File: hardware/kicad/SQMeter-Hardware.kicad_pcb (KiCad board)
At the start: 2 copper layers, 125 x 82 mm, 62 parts, among them J1 12V IN, J10 AUX, J2 USB-C, J3 I2C TSL2591, J4 I2C MLX90614, J5 I2C BME280, J6 I2C SPARE, J7 GPS, J8 RG-15, J9 WIND, Q1 AO3401A, SW1 RESET, SW2 BOOT, U1 AP63203WU, U2 USBLC6-2SC6, U3 ESP32-S3-WROOM-1-N16R8, U4 USBLC6-2SC6, U5 USBLC6-2SC6, U6 USBLC6-2SC6

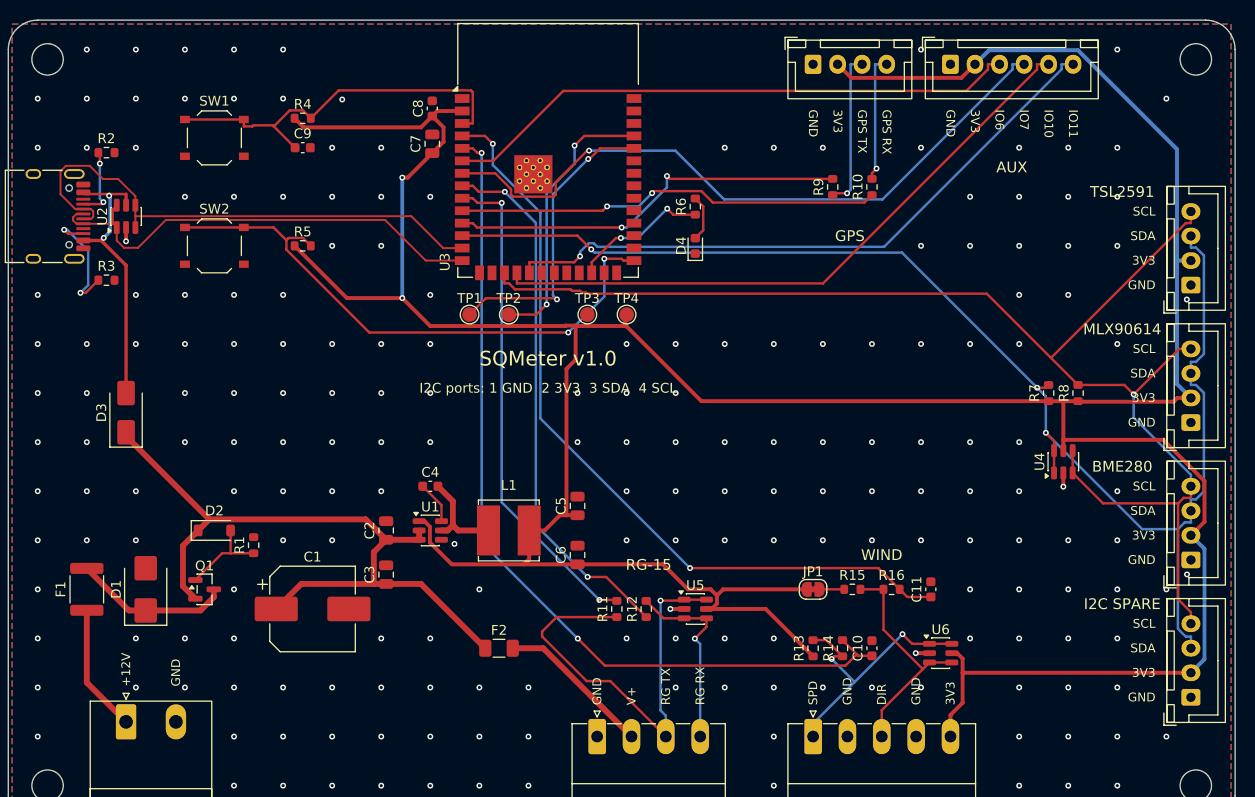
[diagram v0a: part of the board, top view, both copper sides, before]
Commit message: feat: DevKitC-1 socket variant, verified LCSC parts, JLC fab exports
- SQM_VARIANT=devkit swaps the soldered module for ESP32-S3-DevKitC-1 sockets
  (header geometry from Espressif's DXF), 5 V buck feeding the DevKit 5V pin,
  antenna keepout and silkscreen outline
- every part has an in-stock LCSC number; polyfuses moved to 24 V parts
- export_jlc.sh writes gerber zip, BOM and CPL per variant
- build retries routing until DRC has no unconnected or dangling items
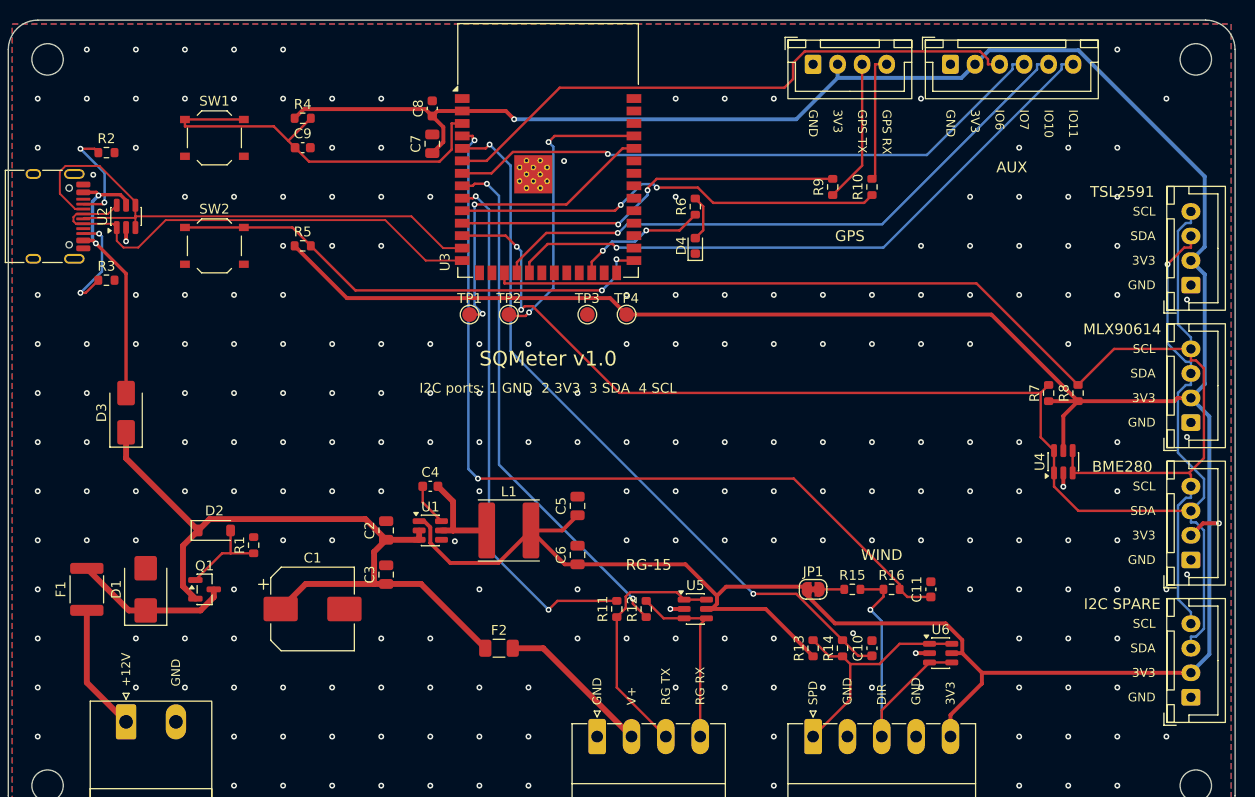
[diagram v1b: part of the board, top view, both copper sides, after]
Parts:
- C1: footprint Capacitor_SMD:CP_Elec_8x10.5 -> Capacitor_SMD:CP_Elec_8x10
- F1: value 1.5A -> 1.5A 24V
- F2: value 0.5A -> 0.5A 24V
- L1: value 4.7u 3A -> 4.7u 3.3A; footprint Inductor_SMD:L_Bourns_SRN6045TA -> Inductor_SMD:L_Sunlord_SWPA6045S
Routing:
- net +3V3: track 369.3 -> 392.7 mm
- net /RG_TXO: track 44.4 -> 25.4 mm, vias 1 -> 0
- net /WIND_SPD: track 89.4 -> 74.6 mm
- net /BOOT: track 59.1 -> 50.8 mm
- net /WIND_DIR: track 80.8 -> 88.2 mm
- net /AUX2: track 69.3 -> 62.4 mm
- net /WDIR_EXT: track 24.0 -> 30.2 mm, vias 0 -> 1
- net /SDA: track 140.4 -> 144.5 mm
- net /RG_RX: track 50.6 -> 54.0 mm
- net /CC1: track 7.40 -> 10.7 mm
- net /EN: track 39.7 -> 42.9 mm
- net /SCL: track 140.4 -> 137.3 mm, vias 1 -> 0
- net /WSPD_EXT: track 27.9 -> 25.0 mm, vias 2 -> 0
- net /USB_DN: track 55.0 -> 57.4 mm
- net /AUX1: track 59.1 -> 61.2 mm
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
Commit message: feat: Waveshare ESP32-S3-Zero socket variant and one GPIO map for all boards
- SQM_VARIANT=zero: ESP32-S3-Zero-M on 2x9 sockets (Waveshare pinout and
  drawing), same 5 V feed scheme as the DevKit variant
- GPIO map unified across module, DevKit and Zero (limited by the Zero's
  GPIO1-13 headers): RG-15 1/2, wind 4/5, I2C 8/9, GPS 12/13, AUX 6/7/10/11
- fab exports for all three
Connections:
- U3 pad 10: /GPS_TX -> (no net)
- U3 pad 11: /GPS_RX -> (no net)
- U3 pad 20: (no net) -> /GPS_TX
- U3 pad 21: (no net) -> /GPS_RX
- U3 pad 38: (no net) -> /RG_RX
- U3 pad 39: (no net) -> /RG_TX
- U3 pad 8: /RG_TX -> (no net)
- U3 pad 9: /RG_RX -> (no net)
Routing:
- net +3V3: track 392.7 -> 334.6 mm, vias 2 -> 4
- net /RG_TX: track 53.5 -> 72.9 mm
- net /RG_RX: track 54.0 -> 71.1 mm, vias 2 -> 4
- net /WIND_SPD: track 74.6 -> 89.0 mm
- net /SCL: track 137.3 -> 149.8 mm
- net /WIND_DIR: track 88.2 -> 77.8 mm
- net /AUX1: track 61.2 -> 68.8 mm, vias 0 -> 2
- net /GPS_RX: track 40.2 -> 33.0 mm
- net /BOOT: track 50.8 -> 57.7 mm
- net /EN: track 42.9 -> 36.2 mm
- net /WDIR_EXT: track 30.2 -> 23.9 mm
- net /U0RXD: track 31.5 -> 25.6 mm
- net /GPS_TX: track 44.0 -> 38.4 mm, vias 2 -> 0
- net /U0TXD: track 29.8 -> 34.9 mm
- net /AUX3: track 63.9 -> 67.9 mm, vias 1 -> 2
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
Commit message: fix: centre boards on the A4 sheet instead of hanging off the page origin
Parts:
- moved C1 107.2 mm to (117.0, 124.0)
- moved C10 107.2 mm to (174.0, 128.0)
- moved C11 107.2 mm to (180.0, 122.0)
- moved C2 107.2 mm to (124.5, 116.0)
- moved C3 107.2 mm to (124.5, 120.5)
- moved C4 107.2 mm to (129.0, 111.5)
- moved C5 107.2 mm to (144.0, 113.5)
- moved C6 107.2 mm to (144.0, 118.5)
- moved C8 107.2 mm to (129.2, 73.0)
- moved C9 107.2 mm to (116.0, 77.0)
- moved D1 107.2 mm to (100.0, 122.0)
- moved D2 107.2 mm to (107.0, 116.0)
- moved D3 107.2 mm to (98.0, 104.0)
- moved D4 107.2 mm to (156.0, 87.0)
- moved F1 107.2 mm to (94.0, 122.0)
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
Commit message: feat: second I2C bus for a second TSL2591 (SQM + SQM-L)
TSL2591 has a fixed address, so the second sensor gets its own bus on
GPIO10/11 (I2C-2 JST-XH port, own pull-ups and ESD). AUX drops to IO6/IO7.
Q1 gate zener replaced by a resistor divider (one fewer extended part).
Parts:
- removed D2: BZT52C10, Diode_SMD:D_SOD-123
- added J13: I2C-2 TSL2591 #2, Connector_JST:JST_XH_B4B-XH-A_1x04_P2.50mm_Vertical, F.Cu at (195.0, 68.5)
- added R19: 10k, Resistor_SMD:R_0603_1608Metric, F.Cu at (107.0, 115.0)
- added R20: 4.7k, Resistor_SMD:R_0603_1608Metric, F.Cu at (185.0, 82.5)
- added R21: 4.7k, Resistor_SMD:R_0603_1608Metric, F.Cu at (188.0, 82.5)
- added U7: USBLC6-2SC6, Package_TO_SOT_SMD:SOT-23-6, F.Cu at (192.0, 85.0)
- J10: footprint Connector_JST:JST_XH_B6B-XH-A_1x06_P2.50mm_Vertical -> Connector_JST:JST_XH_B4B-XH-A_1x04_P2.50mm_Vertical
- J3: value I2C TSL2591 -> I2C TSL2591 #1
- moved H2 7.52 mm to (207.5, 75.5)
- moved J10 0.50 mm to (181.5, 68.5)
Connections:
- U3 pad 18: /AUX3 -> /SDA2
- U3 pad 19: /AUX4 -> /SCL2
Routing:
- net /SDA2: track 0.00 -> 88.8 mm, vias 0 -> 2
- net /SCL2: track 0.00 -> 86.3 mm
- net /AUX3: track 67.9 -> 0.00 mm, vias 2 -> 0
- net /AUX4: track 67.5 -> 0.00 mm, vias 1 -> 0
- net +3V3: track 334.6 -> 353.0 mm, vias 4 -> 6
- net /RG_TX: track 72.9 -> 55.6 mm
- net /WIND_DIR: track 77.8 -> 94.7 mm
- net /RG_RX: track 71.1 -> 55.8 mm, vias 4 -> 2
- net /EN: track 36.2 -> 51.2 mm
- net /SCL: track 149.8 -> 138.8 mm, vias 0 -> 1
- net /AUX1: track 68.8 -> 58.6 mm, vias 2 -> 1
- net /SDA: track 148.3 -> 142.0 mm
- net /WIND_SPD: track 89.0 -> 82.8 mm
- net /U0TXD: track 34.9 -> 30.2 mm
- net /BOOT: track 57.7 -> 53.3 mm
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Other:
- board text added: "I2C-2"
- board text added: "TSL2591 #1"
- board text removed: "IO10"
- board text removed: "IO11"
- board text removed: "TSL2591"

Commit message: feat: brand lockup on silkscreen, hardware Rev A, JLC-ready gerber zips
- SQMeter lockup (brand kit silkscreen mark + Inter SemiBold name) as plain
  silkscreen polygons from brand_silk.json; no font install needed
- HW_REV = A: on the silkscreen, KiCad title blocks, gerber metadata and fab
  file names; versioned separately from firmware
- drop the verbose I2C pinout line; per-pin labels already cover it
- gerber zip holds only fab layers + drill files
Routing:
- net /SCL: track 138.8 -> 155.4 mm, vias 1 -> 0
- net /SCL2: track 86.3 -> 99.0 mm, vias 0 -> 1
- net /WIND_SPD: track 82.8 -> 94.9 mm
- net +3V3: track 353.0 -> 363.1 mm, vias 6 -> 5
- net /GPS_TX: track 39.4 -> 48.1 mm, vias 0 -> 2
- net /WIND_DIR: track 94.7 -> 86.9 mm
- net /RG_RXI: track 23.2 -> 30.7 mm
- net /EN: track 51.2 -> 45.3 mm
- net /RG_TXO: track 28.1 -> 23.7 mm, vias 0 -> 1
- net /AUX1: track 58.6 -> 62.4 mm, vias 1 -> 0
- net /U0TXD: track 30.2 -> 26.7 mm
- net /U0RXD: track 25.5 -> 28.7 mm
- net /BOOT: track 53.3 -> 50.3 mm
- net /RG_RX: track 55.8 -> 53.7 mm
- net /WSPD_EXT: track 28.0 -> 26.1 mm
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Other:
- board text added: "Rev A ESP32-S3 module"
- board text removed: "I2C ports: 1 GND 2 3V3 3 SDA 4 SCL"
- board text removed: "SQMeter v1.0"

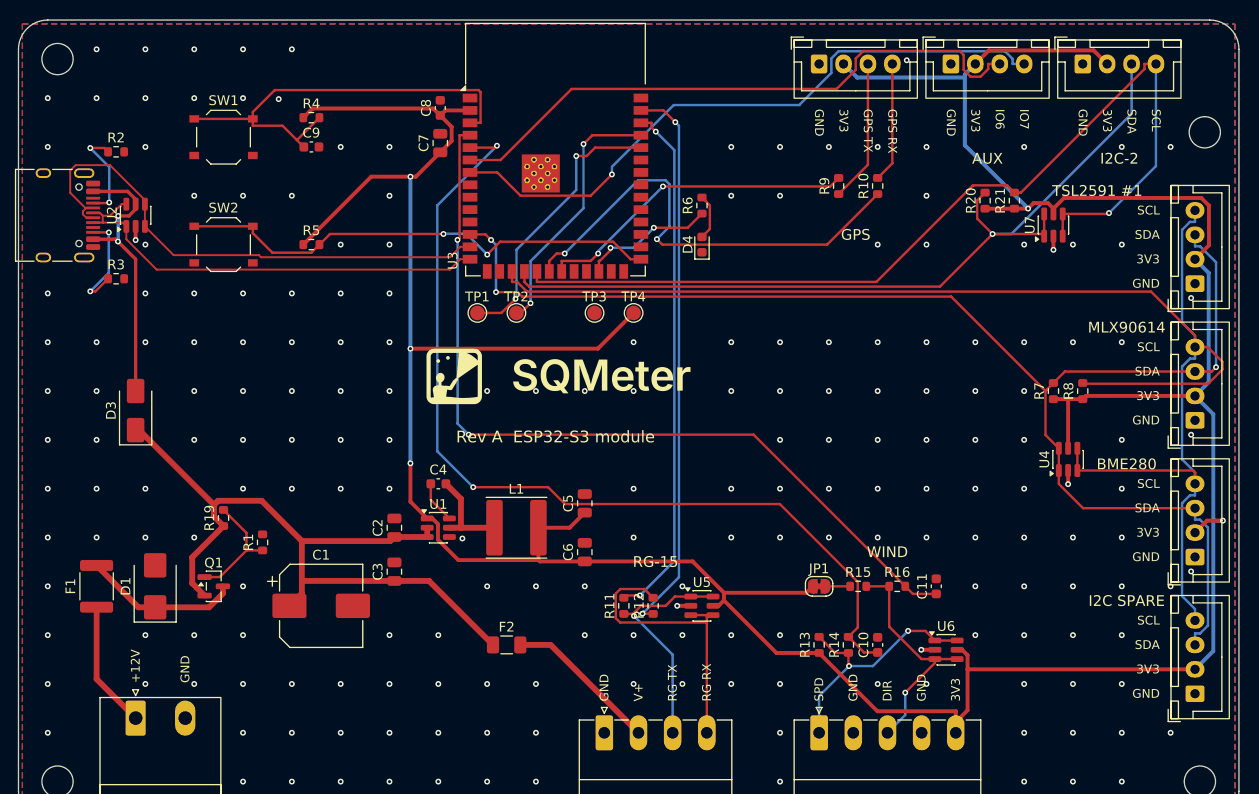
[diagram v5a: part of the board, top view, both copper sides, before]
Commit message: feat: Inter Bold silkscreen (embedded), black mask / white silk stackup
- all silkscreen text and references in Inter Bold, min 1.2 mm; font embedded in
  the board files so they open the same without Inter installed
- stroke widths measured on plotted gerbers (>0.15 mm); KiCad's TrueType
  thickness check ignored as it flags every size of the variable font
- stackup: black solder mask, white silkscreen (3D view; colour is picked at order)
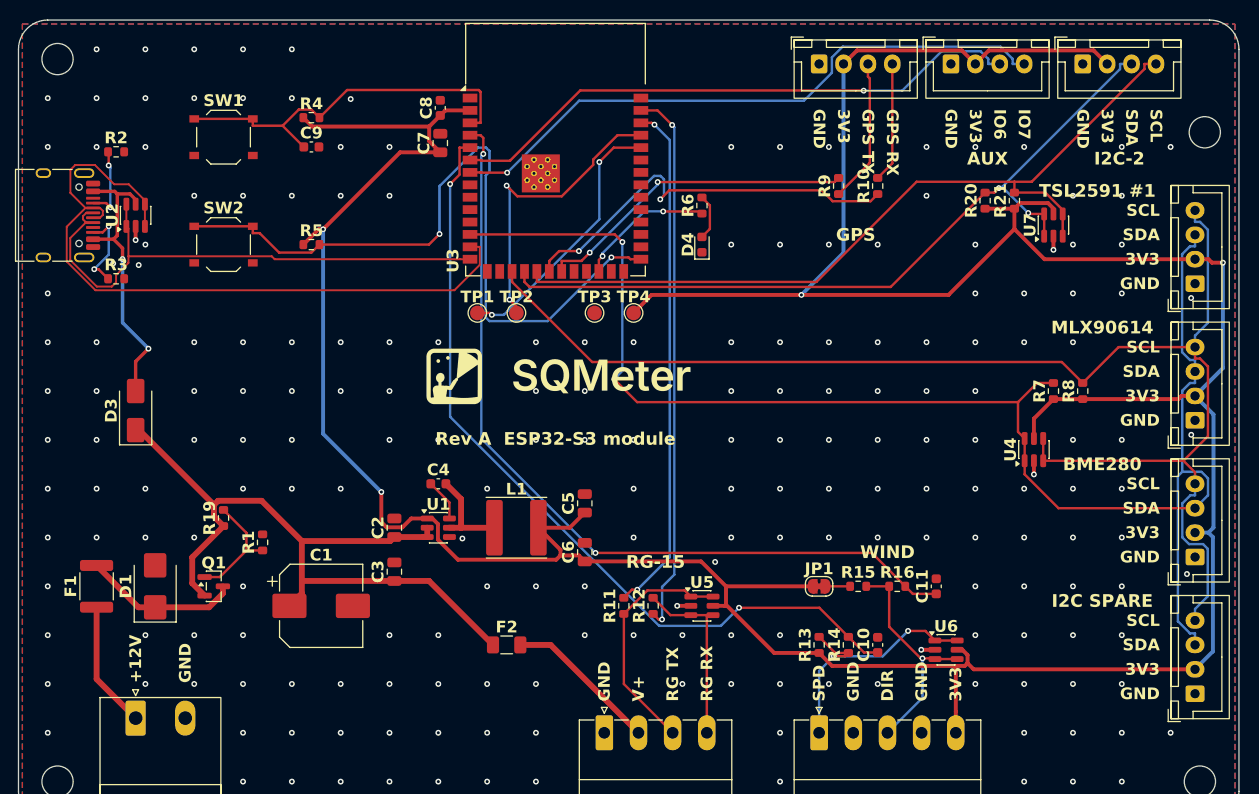
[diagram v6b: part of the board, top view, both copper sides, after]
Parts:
- moved U4 3.64 mm to (190.0, 108.0)
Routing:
- net +3V3: track 363.1 -> 388.9 mm, vias 5 -> 4
- net /BOOT: track 50.3 -> 75.3 mm
- net /USB_DN: track 54.7 -> 73.7 mm
- net /SCL2: track 99.0 -> 83.5 mm, vias 1 -> 0
- net /SDA: track 142.4 -> 155.9 mm, vias 3 -> 2
- net /SCL: track 155.4 -> 142.5 mm
- net /RG_RXI: track 30.7 -> 18.9 mm
- net /WIND_SPD: track 94.9 -> 84.4 mm
- net /USB_DP: track 46.5 -> 57.0 mm
- net /SDA2: track 88.7 -> 81.0 mm, vias 1 -> 2
- net /GPS_TX: track 48.1 -> 42.2 mm
- net /EN: track 45.3 -> 39.6 mm
- net /U0TXD: track 26.7 -> 30.6 mm
- net /AUX1: track 62.4 -> 59.8 mm, vias 0 -> 1
- net /CC1: track 10.0 -> 7.75 mm
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
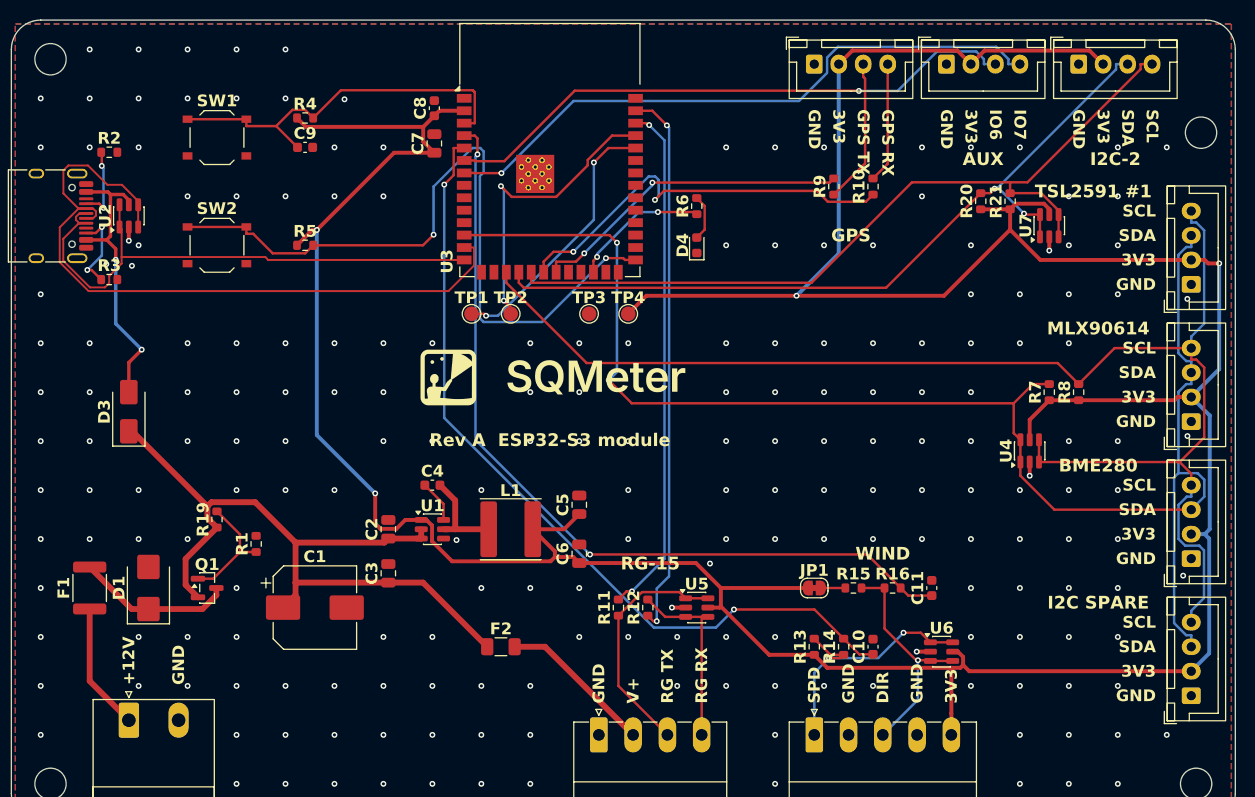
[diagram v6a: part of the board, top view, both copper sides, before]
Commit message: feat: ESP32-S3-ETH PoE home board and Li-ion travel board
- eth: Waveshare ESP32-S3-ETH (+ PoE module) on 2x20 sockets, PoE or 12 V in,
  MT3608 boost keeps the RG-15 at 12.6 V on PoE; own GPIO map (W5500 owns 9-14)
- travel: ESP32-S3-Zero, USB-C only, MCP73871 power-path Li-ion charger with
  NTC cold-charge cut-off, power slide switch, battery/charger status on GPIO,
  OLED port; 85 x 66 mm, no field wiring
- connector titles placed relative to their connector so layouts can differ
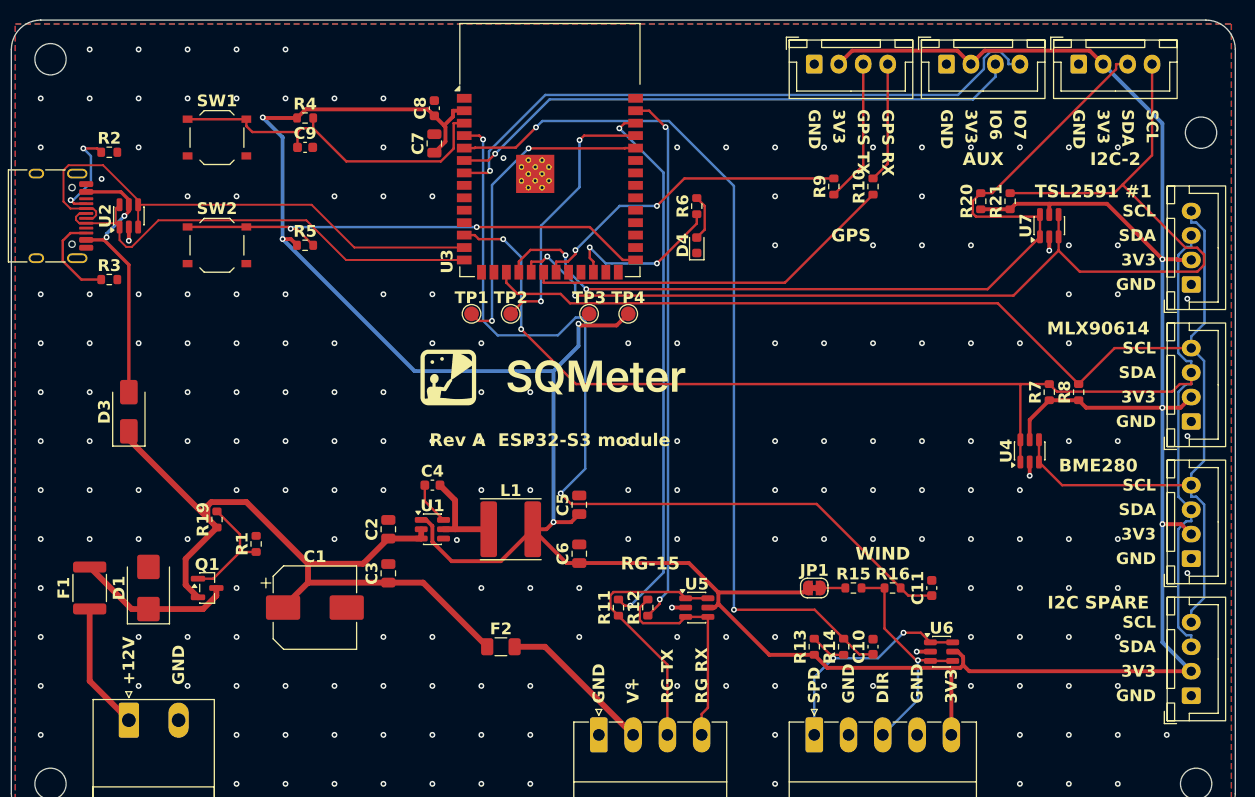
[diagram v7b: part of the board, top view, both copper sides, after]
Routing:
- net /SCL2: track 83.5 -> 116.8 mm, vias 0 -> 2
- net +3V3: track 388.9 -> 359.4 mm, vias 4 -> 7
- net /BOOT: track 75.3 -> 50.3 mm
- net /USB_DN: track 73.7 -> 55.7 mm
- net /SDA: track 155.9 -> 141.4 mm
- net /SDA2: track 81.0 -> 91.9 mm
- net /USB_DP: track 57.0 -> 47.9 mm
- net /WIND_DIR: track 85.5 -> 93.4 mm
- net /WIND_SPD: track 84.4 -> 90.8 mm
- net /U0RXD: track 27.4 -> 32.5 mm
- net /GPS_TX: track 42.2 -> 38.4 mm, vias 2 -> 0
- net /RG_RXI: track 18.9 -> 22.1 mm
- net /EN: track 39.6 -> 36.5 mm
- net /U0TXD: track 30.6 -> 27.6 mm
- net /LED: track 14.1 -> 16.9 mm
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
